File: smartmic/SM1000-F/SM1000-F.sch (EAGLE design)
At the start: 215 parts, among them CN1 HDR100-3, CN10 ST-3509, CN11 HDR100-3, CN112 DIL16X300, CN2 JS-MU3-002, CN3 DS-0518, CN4 RJ-45, CN5 ST-3509, CN6 ST-3509, CN7 ST-3509, CN8 ST-3509, CN9 ST-3509, J1 JMP-2PIN, J2 JMP-2PIN, J3 JMP-2PIN, J4 CONN-BOOM-XH-2A, J5 JMP-2PIN, P1 TPAD50, P10 TPAD50, P11 TPAD50, P12 TPAD50, P13 TPAD50, P14 TPAD50, P15 TPAD50, P16 TPAD50, P17 TPAD50, P18 TPAD50, P19 TPAD50, P2 TPAD50, P20 TPAD50, P21 TPAD50, P3 TPAD50, P4 TPAD50, P5 TPAD50, P6 TPAD50, P7 TPAD50, P8 TPAD50, P9 TPAD50, SW1 SW-LC2259, SW2 TS-026, SW3 SW-LC2259EENP, SW4 TS-026, SW5 TS-02B, T1 SM-LP-5001, T2 SM-LP-5001, U1 STM32F405VGT6, U10 24LC256-I/MS, U2 LD3985M33R, U3 STMPS2141, U4 EMIF02-USB03F2, U5 TPS54329E, U6 LMV341, U7 LMV341, U8 LM386M-1, U9 LMV341

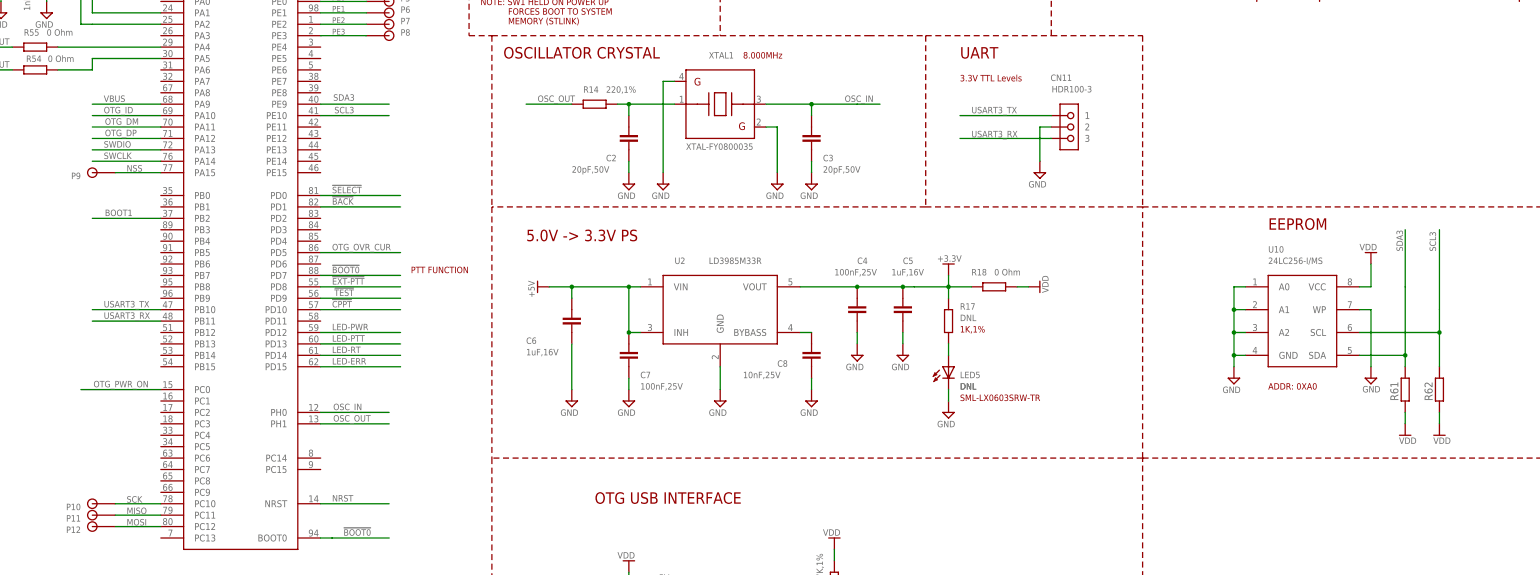
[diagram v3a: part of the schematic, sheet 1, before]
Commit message: ADD PDFs of Schematics and board layers L1, L2, L3 & L4 for reference only. RGB 10/03/15
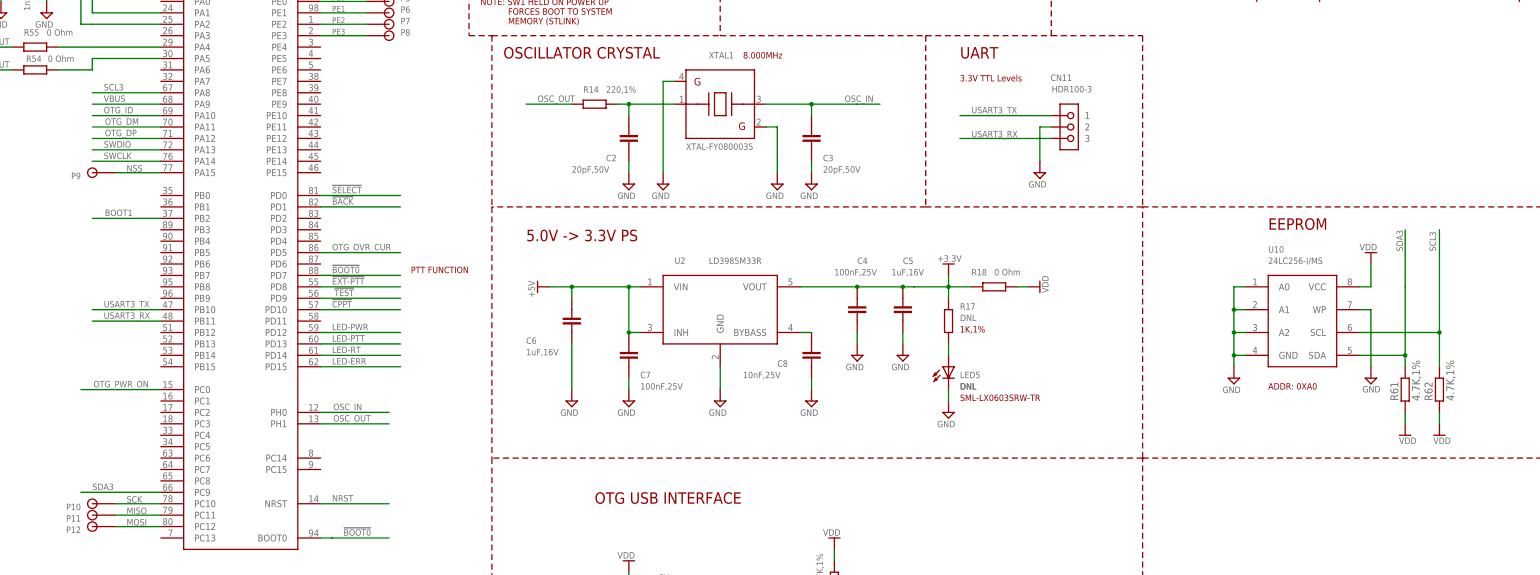
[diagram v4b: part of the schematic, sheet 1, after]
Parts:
- removed R59: (no value), AA-ipc-7351-resistor:RESISTOR_1206
- R61, R62: value (none) -> 4.7K,1%
- U10: device coherix:I2C-EEPROM-256KMSOP-8 -> _RoweTel:I2C-EEPROM-256K
- renumbered CN112 to CN12
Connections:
- net SCL3: now also U1A.PA8; no longer U1A.PE10
- net SDA3: now also U1A.PC9; no longer U1A.PE9
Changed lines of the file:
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@@
 <part name="V143" library="A-SUPPLY2" deviceset="GND" device=""/>
 <part name="D8" library="_RoweTel" deviceset="PESD5ZX" device="" value="DNL"/>
-<part name="CN112" library="_RoweTel" deviceset="DIL16X300" device=""/>
-<part name="R59" library="AA-ipc-7351-resistor" deviceset="RESISTOR_" device="1206"/>
+<part name="CN12" library="_RoweTel" deviceset="DIL16X300" device=""/>
 <part name="R60" library="AA-ipc-7351-resistor" deviceset="RESISTOR_" device="1206" value="330,1%"/>
 <part name="J5" library="_Coherix" deviceset="JMP-2PIN" device=""/>
@@
 <part name="V144" library="A-SUPPLY2" deviceset="GND" device=""/>
 <part name="P21" library="_Coherix" deviceset="TPAD50" device=""/>
-<part name="U10" library="coherix" deviceset="I2C-EEPROM-256K" device="MSOP-8" value="24LC256-I/MS"/>
+<part name="U10" library="_RoweTel" deviceset="I2C-EEPROM-256K" device="" value="24LC256-I/MS"/>
 <part name="V145" library="A-SUPPLY2" deviceset="GND" device=""/>
 <part name="V146" library="A-SUPPLY2" deviceset="GND" device=""/>
 <part name="V147" library="A-SUPPLY2" deviceset="VDD" device=""/>
-<part name="R61" library="AA-ipc-7351-resistor" deviceset="RESISTOR_" device="0603"/>
-<part name="R62" library="AA-ipc-7351-resistor" deviceset="RESISTOR_" device="0603"/>
+<part name="R61" library="AA-ipc-7351-resistor" deviceset="RESISTOR_" device="0603" value="4.7K,1%"/>
+<part name="R62" library="AA-ipc-7351-resistor" deviceset="RESISTOR_" device="0603" value="4.7K,1%"/>
 <part name="V148" library="A-SUPPLY2" deviceset="VDD" device=""/>
 <part name="V149" library="A-SUPPLY2" deviceset="VDD" device=""/>
@@
 <net name="SDA3" class="0">
 <segment>
-<pinref part="U1" gate="A" pin="PE9"/>
-<wire x1="147.32" y1="195.58" x2="162.56" y2="195.58" width="0.1524" layer="91"/>
-<label x="150.114" y="196.342" size="1.4224" layer="95" ratio="10"/>
-</segment>
-<segment>
 <wire x1="378.46" y1="139.7" x2="388.62" y2="139.7" width="0.1524" layer="91"/>
 <wire x1="388.62" y1="139.7" x2="388.62" y2="154.94" width="0.1524" layer="91"/>
@@
 <junction x="388.62" y="139.7"/>
 </segment>
-</net>
-<net name="SCL3" class="0">
 <segment>
-<pinref part="U1" gate="A" pin="PE10"/>
-<wire x1="147.32" y1="193.04" x2="162.56" y2="193.04" width="0.1524" layer="91"/>
-<label x="150.368" y="193.548" size="1.4224" layer="95" ratio="10"/>
+<pinref part="U1" gate="A" pin="PC9"/>
+<wire x1="111.76" y1="109.22" x2="93.98" y2="109.22" width="0.1524" layer="91"/>
+<label x="96.52" y="109.728" size="1.4224" layer="95" ratio="10"/>
 </segment>
+</net>
+<net name="SCL3" class="0">
 <segment>
 <wire x1="378.46" y1="144.78" x2="396.24" y2="144.78" width="0.1524" layer="91"/>
@@
 <junction x="396.24" y="144.78"/>
 </segment>
+<segment>
+<pinref part="U1" gate="A" pin="PA8"/>
+<wire x1="111.76" y1="198.12" x2="96.52" y2="198.12" width="0.1524" layer="91"/>
+<label x="99.06" y="198.628" size="1.4224" layer="95" ratio="10"/>
+</segment>
 </net>
 </nets>
@@
 <attribute name="VALUE" x="45.72" y="119.38" size="1.4224" layer="96" ratio="10"/>
 </instance>
-<instance part="CN112" gate="G$1" x="317.5" y="182.88" smashed="yes">
+<instance part="CN12" gate="G$1" x="317.5" y="182.88" smashed="yes">
 <attribute name="NAME" x="312.42" y="196.596" size="1.4224" layer="95" ratio="10"/>
 <attribute name="VALUE" x="312.42" y="170.18" size="1.4224" layer="96" ratio="10"/>
 </instance>
-<instance part="R59" gate="G$1" x="401.32" y="106.68"/>
 <instance part="R60" gate="G$1" x="269.24" y="124.46" smashed="yes" rot="R180">
 <attribute name="NAME" x="262.128" y="125.476" size="1.4224" layer="95" ratio="9"/>
@@
 <pinref part="CN4" gate="G$1" pin="8"/>
 <wire x1="327.66" y1="193.04" x2="325.12" y2="193.04" width="0.1524" layer="91"/>
-<pinref part="CN112" gate="G$1" pin="8"/>
+<pinref part="CN12" gate="G$1" pin="8"/>
 <pinref part="P15" gate="G$1" pin="1"/>
 <junction x="327.66" y="193.04"/>
@@
 <pinref part="CN4" gate="G$1" pin="7"/>
 <wire x1="327.66" y1="190.5" x2="325.12" y2="190.5" width="0.1524" layer="91"/>
-<pinref part="CN112" gate="G$1" pin="7"/>
+<pinref part="CN12" gate="G$1" pin="7"/>
 </segment>
 </net>
@@
 <pinref part="CN4" gate="G$1" pin="6"/>
 <wire x1="327.66" y1="187.96" x2="325.12" y2="187.96" width="0.1524" layer="91"/>
-<pinref part="CN112" gate="G$1" pin="6"/>
+<pinref part="CN12" gate="G$1" pin="6"/>
 </segment>
 </net>
@@
 <pinref part="CN4" gate="G$1" pin="5"/>
 <wire x1="327.66" y1="185.42" x2="325.12" y2="185.42" width="0.1524" layer="91"/>
-<pinref part="CN112" gate="G$1" pin="5"/>
+<pinref part="CN12" gate="G$1" pin="5"/>
 </segment>
 </net>
@@
 <pinref part="CN4" gate="G$1" pin="4"/>
 <wire x1="327.66" y1="182.88" x2="325.12" y2="182.88" width="0.1524" layer="91"/>
-<pinref part="CN112" gate="G$1" pin="4"/>
+<pinref part="CN12" gate="G$1" pin="4"/>
 </segment>
 </net>
@@
 <pinref part="CN4" gate="G$1" pin="3"/>
 <wire x1="327.66" y1="180.34" x2="325.12" y2="180.34" width="0.1524" layer="91"/>
-<pinref part="CN112" gate="G$1" pin="3"/>
+<pinref part="CN12" gate="G$1" pin="3"/>
 </segment>
 </net>
@@
 <pinref part="CN4" gate="G$1" pin="2"/>
 <wire x1="327.66" y1="177.8" x2="325.12" y2="177.8" width="0.1524" layer="91"/>
-<pinref part="CN112" gate="G$1" pin="2"/>
+<pinref part="CN12" gate="G$1" pin="2"/>
 </segment>
 </net>
@@
 <pinref part="CN4" gate="G$1" pin="1"/>
 <wire x1="327.66" y1="175.26" x2="325.12" y2="175.26" width="0.1524" layer="91"/>
-<pinref part="CN112" gate="G$1" pin="1"/>
+<pinref part="CN12" gate="G$1" pin="1"/>
 </segment>
 </net>
@@
 <wire x1="332.74" y1="96.52" x2="330.2" y2="96.52" width="0.1524" layer="91"/>
 <wire x1="330.2" y1="96.52" x2="297.18" y2="96.52" width="0.1524" layer="91"/>
-<pinref part="CN112" gate="G$1" pin="15"/>
+<pinref part="CN12" gate="G$1" pin="15"/>
 </segment>
 </net>
@@
 <pinref part="CN6" gate="G$1" pin="D"/>
 <wire x1="299.72" y1="142.24" x2="325.12" y2="142.24" width="0.1524" layer="91"/>
-<pinref part="CN112" gate="G$1" pin="P16"/>
+<pinref part="CN12" gate="G$1" pin="P16"/>
 </segment>
 </net>
@@
 <wire x1="325.12" y1="55.88" x2="325.12" y2="63.5" width="0.1524" layer="91"/>
 <junction x="325.12" y="63.5"/>
-<pinref part="CN112" gate="G$1" pin="14"/>
+<pinref part="CN12" gate="G$1" pin="14"/>
 </segment>
 </net>
@@
 <wire x1="274.32" y1="185.42" x2="274.32" y2="182.88" width="0.1524" layer="91"/>
 <pinref part="V133" gate="G$1" pin="RF_MIC"/>
-<pinref part="CN112" gate="G$1" pin="11"/>
+<pinref part="CN12" gate="G$1" pin="11"/>
 </segment>
 <segment>
@@
 <junction x="266.7" y="190.5"/>
 <pinref part="V134" gate="G$1" pin="RF_SPKR"/>
-<pinref part="CN112" gate="G$1" pin="9"/>
-<pinref part="CN112" gate="G$1" pin="10"/>
+<pinref part="CN12" gate="G$1" pin="9"/>
+<pinref part="CN12" gate="G$1" pin="10"/>
 </segment>
 <segment>
@@
 <wire x1="281.94" y1="185.42" x2="281.94" y2="182.88" width="0.1524" layer="91"/>
 <junction x="281.94" y="182.88"/>
-<pinref part="CN112" gate="G$1" pin="12"/>
-<pinref part="CN112" gate="G$1" pin="13"/>
+<pinref part="CN12" gate="G$1" pin="12"/>
+<pinref part="CN12" gate="G$1" pin="13"/>
 </segment>
 </net>
